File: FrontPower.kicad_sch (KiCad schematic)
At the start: 18 parts, among them SW1 Main switch - consumption

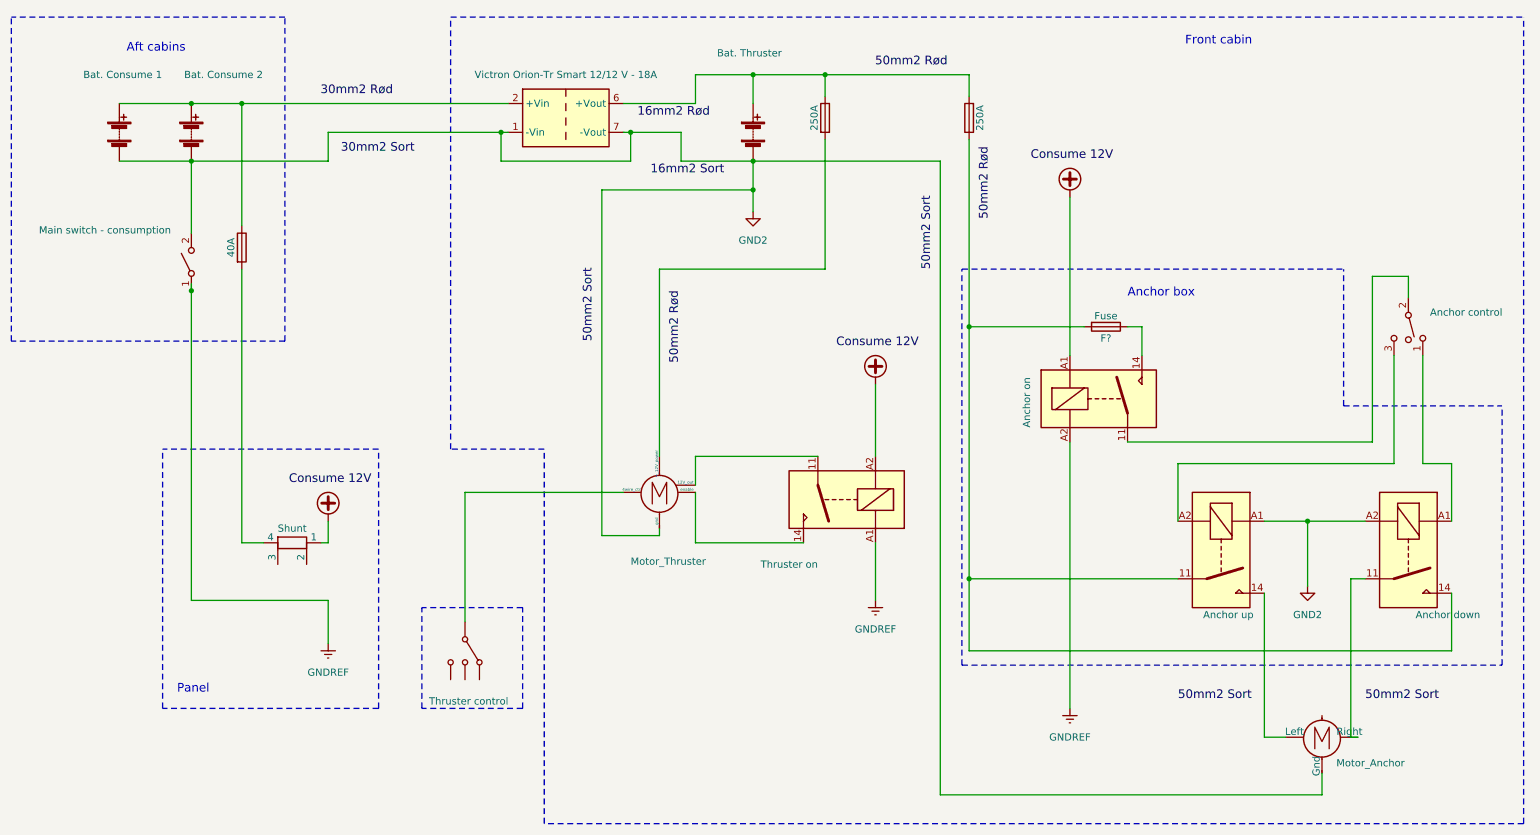
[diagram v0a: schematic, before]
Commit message: FrontPower version 2.1
Back to charging thruster battery from house-bank.

Victron will have a very low threshold to ensure there is enough
time to charge thruster battery - even if house bank is low.
(In the past, the problem was that a low house bank caused input voltage
at Victron to never reach the threshold)

Drawback of always keeping Vicron 'alive' is that it will always drain
on house bank. Hope is that the drain will be negligble when thruster has
fully charged.
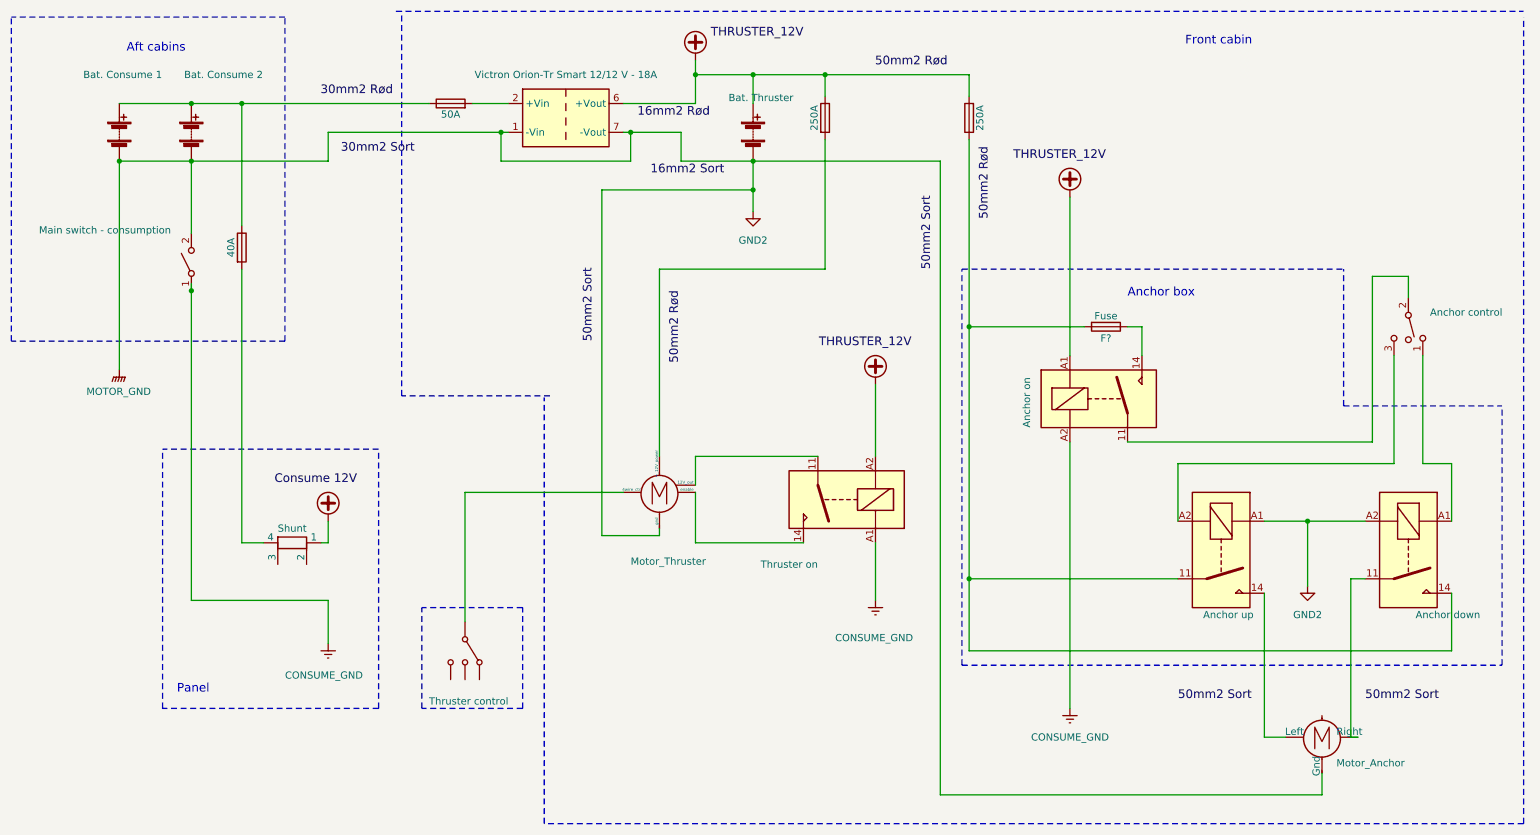
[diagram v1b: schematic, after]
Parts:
- added F1: 50A, symbol FrontPower-rescue:Fuse
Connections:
- net +VDC: now also BT?.1 (+), F?.1, F?.2, PS1.6 (+Vout)
- net at BT?.1 (+), Bat1.1 (+), F?.1: now also F1.1; no longer PS1.2 (+Vin)
- net GNDREF renamed CONSUME_GND
- new net: F1.2, PS1.2 (+Vin)
